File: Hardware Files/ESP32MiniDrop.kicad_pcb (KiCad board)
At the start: 2 copper layers, 74 x 54 mm, 29 parts, among them J1 0.100" 2x4 Header, J2 Solenoid1 Terminal, J3 AudioJack3, J5 Barrel_Jack_Switch, M1 Conn_01x01, M2 Conn_01x01, M3 Conn_01x01, M4 Conn_01x01, Q1 NMOS 60V 46A, SW1 SPST (BLUE)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

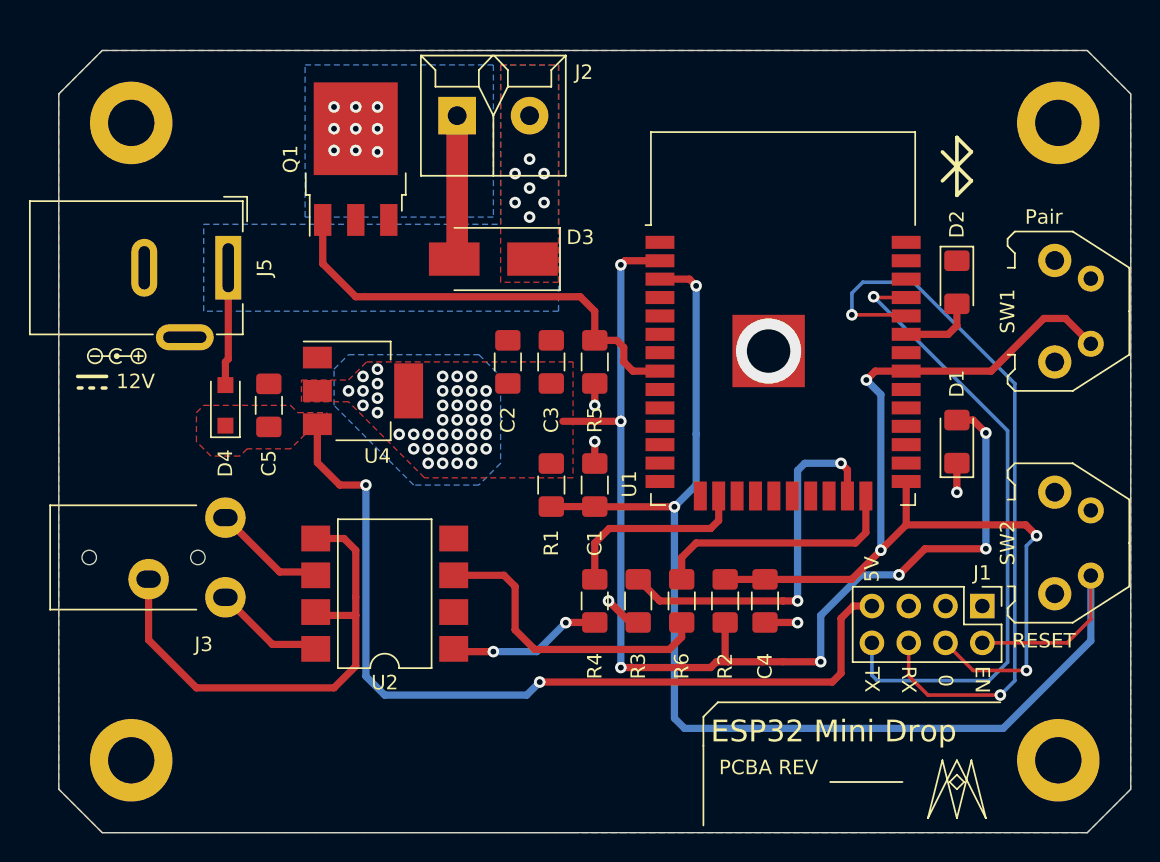
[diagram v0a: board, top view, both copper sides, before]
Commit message: Change Audio Jack to SJ1-3523N
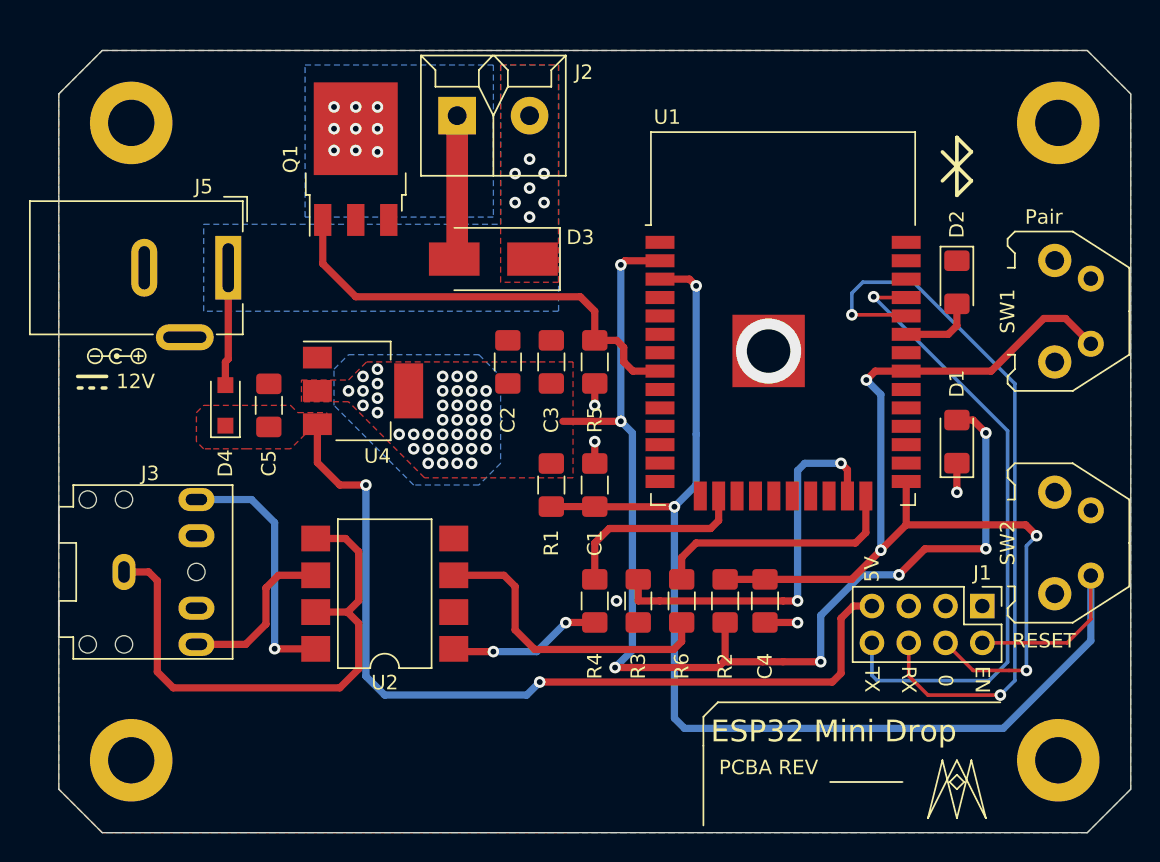
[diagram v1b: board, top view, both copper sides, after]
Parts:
- J3: footprint ESP32MiniDrop_PCB_Library:STX-3000 -> ESP32MiniDrop_PCB_Library:SJ1-3523N
- moved J3 2.24 mm to (9.50, 36.0), turned to 0 degrees
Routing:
- net Net-(J3-PadR): track 7.71 -> 18.0 mm, vias 0 -> 1
- net Net-(J3-PadS): track 34.4 -> 38.3 mm
- net Net-(J3-PadT): track 8.13 -> 12.0 mm
- net GND: track 9.96 -> 7.86 mm
- net +3V3: track 78.8 -> 79.7 mm
- net U0TX_Active: track 26.3 -> 27.1 mm

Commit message: Update 3.3V trace routing
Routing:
- net +3V3: vias 47 -> 45

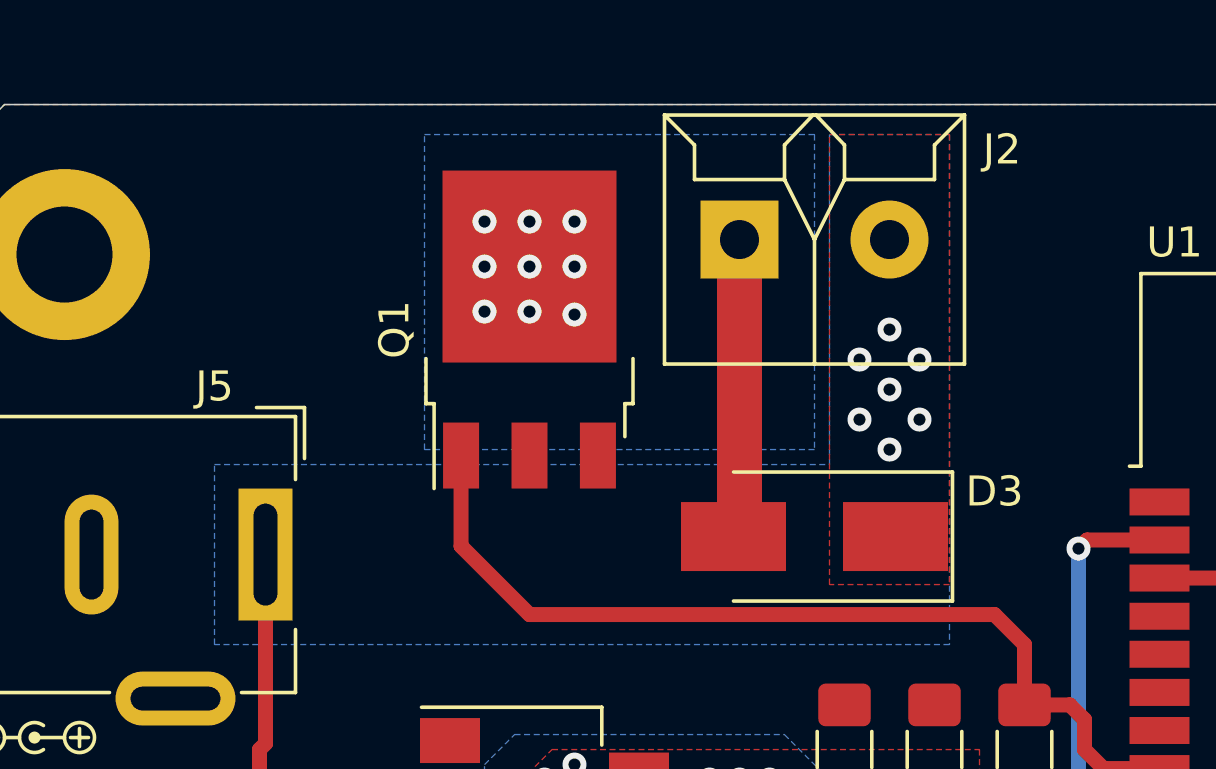
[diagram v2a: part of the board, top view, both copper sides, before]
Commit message: Change libraries to relative project library
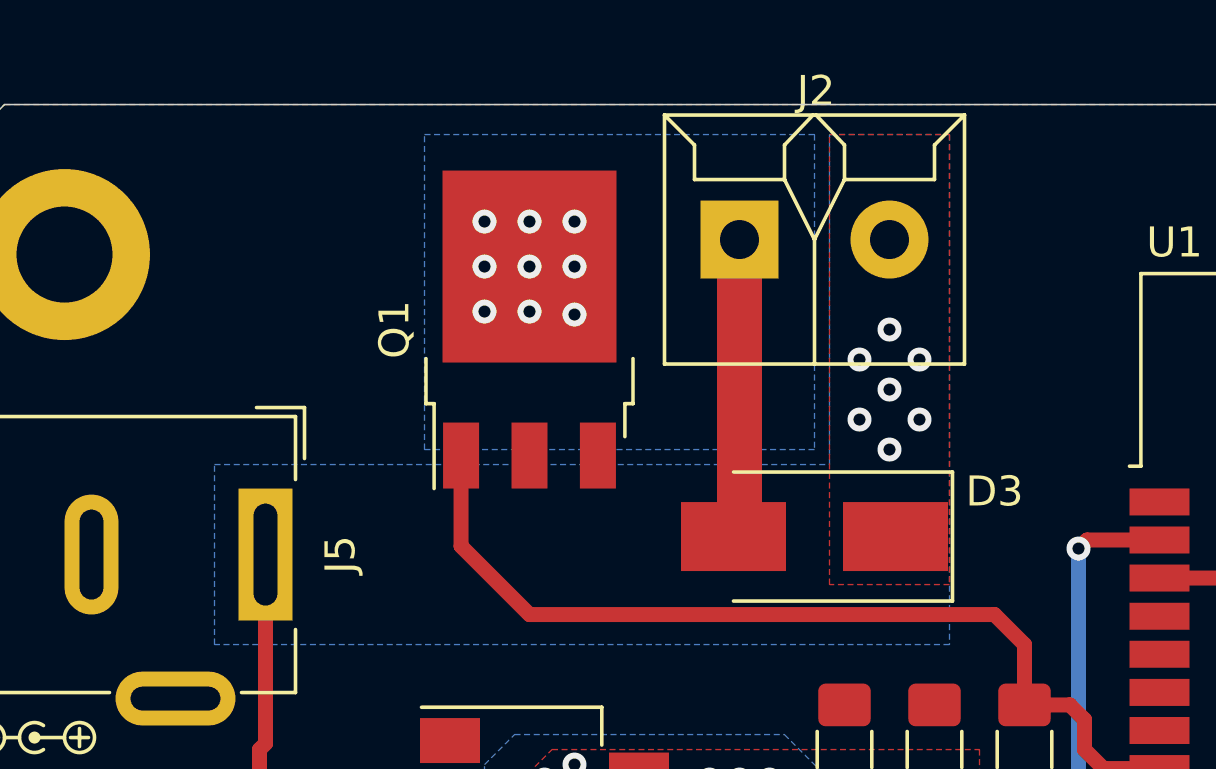
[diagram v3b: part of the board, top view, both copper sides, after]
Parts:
- J2: footprint ESP32MiniDrop_PCB_Library:1935161 -> ESP32MiniDrop:1935161
- J5: footprint ESP32MiniDrop_PCB_Library:BarrelJack_Wuerth_6941xx301002_3D -> ESP32MiniDrop:BarrelJack_Wuerth_6941xx301002_3D
- SW1, SW2: footprint ESP32MiniDrop_PCB_Library:1825027-8 -> ESP32MiniDrop:1825027-8

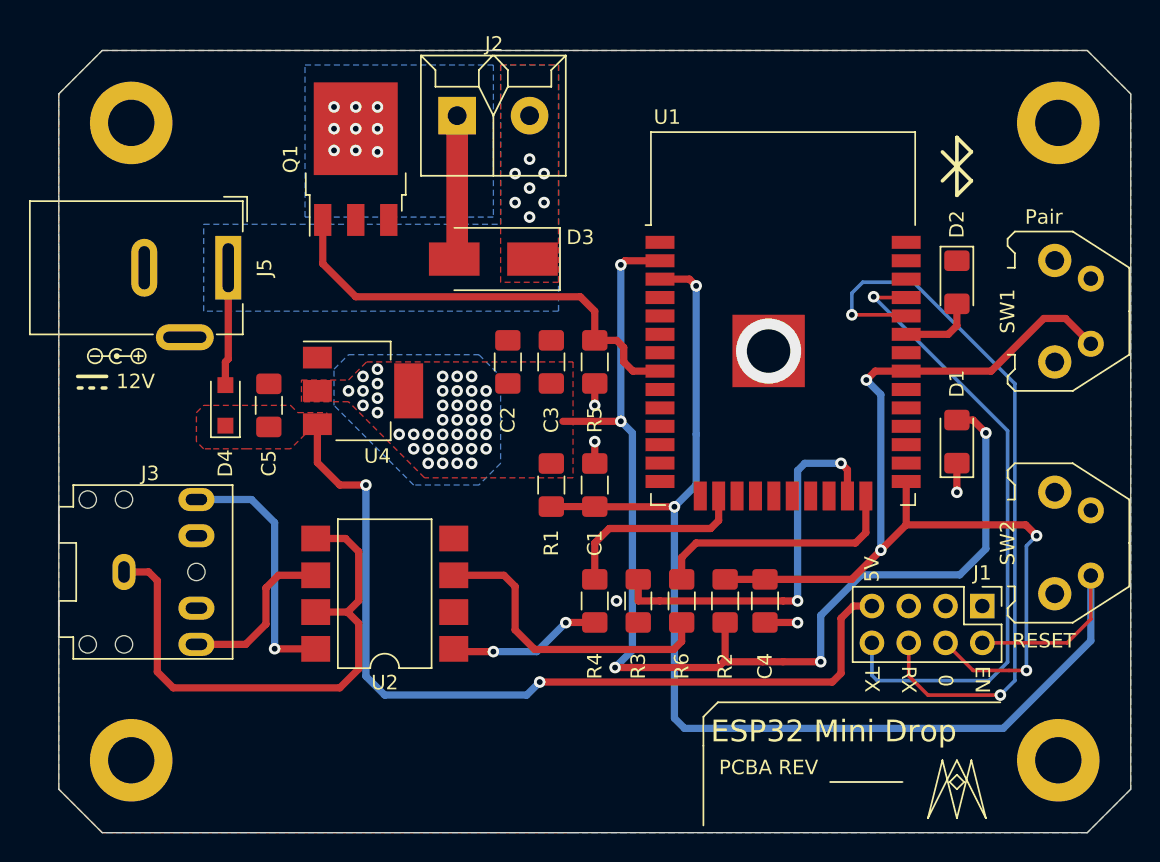
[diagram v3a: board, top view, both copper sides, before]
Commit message: Fix missing library item
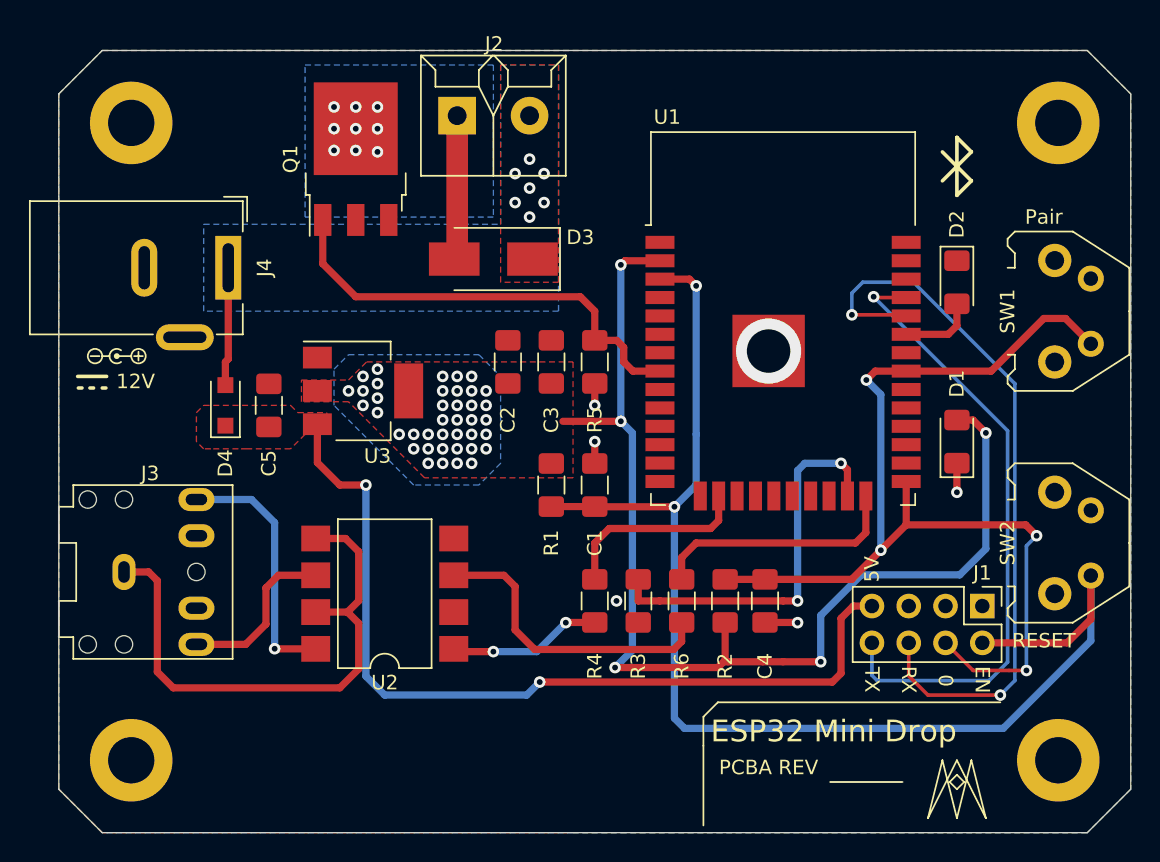
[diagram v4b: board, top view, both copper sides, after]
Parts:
- J3: footprint ESP32MiniDrop_PCB_Library:SJ1-3523N -> ESP32MiniDrop:SJ1-3523N
- renumbered J5 to J4, U4 to U3

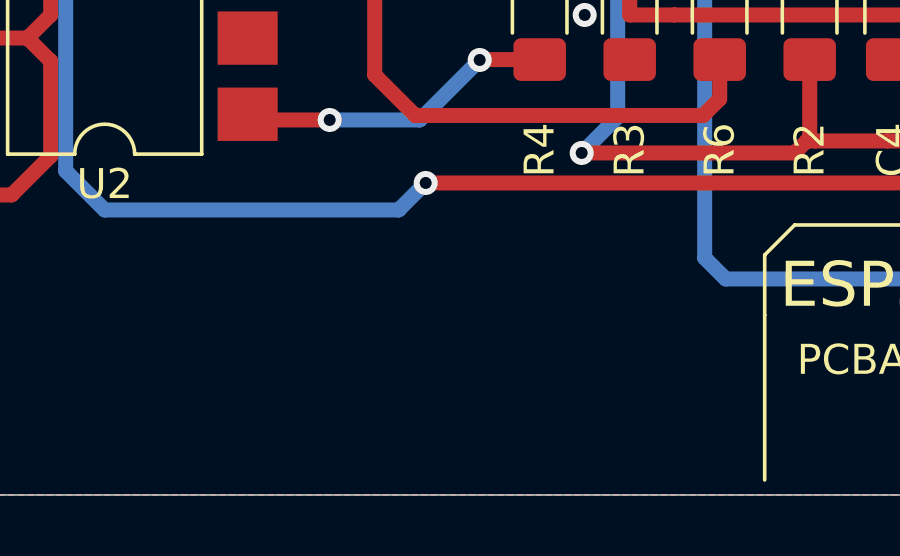
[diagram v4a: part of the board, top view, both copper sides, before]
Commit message: Add logo and update PCBA Rev
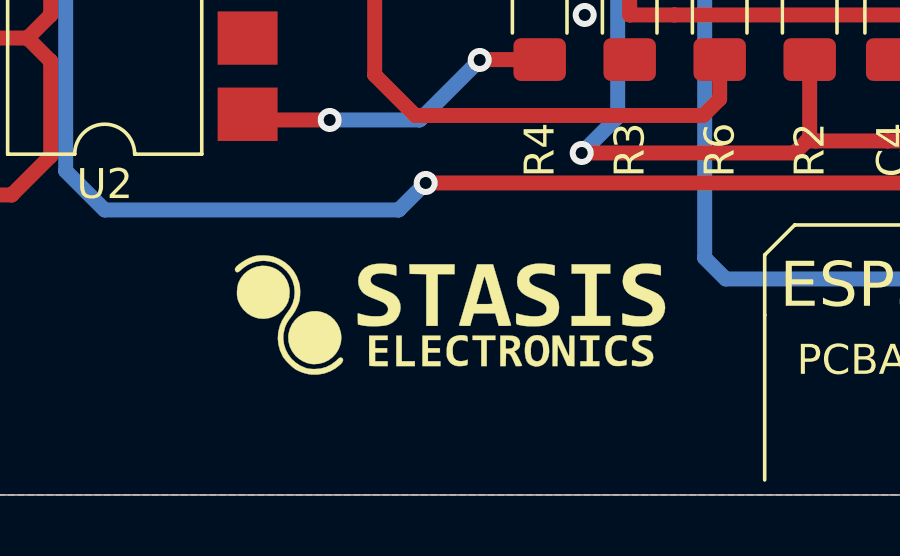
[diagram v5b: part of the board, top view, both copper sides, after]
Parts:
- added G***: LOGO, ESP32MiniDrop:logo, F.Cu at (34.0, 48.0)
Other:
- board text added: "A03"
- board text removed: "A02"
